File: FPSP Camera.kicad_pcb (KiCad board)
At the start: 4 copper layers, 85.7 x 31.1 mm, 72 parts, among them J1 Conn_01x24_Socket, J2 Conn_02x04_Counter_Clockwise, J3 Conn_02x07_Counter_Clockwise, J7 Conn_01x02, U1 ICM-45686, U3 RP2350_60QFN, U4 TLV75533PDRV, U5 TLV73328PDRV, U6 TLV73315PDRV, Y1 SiT8008xx-1x-xxE

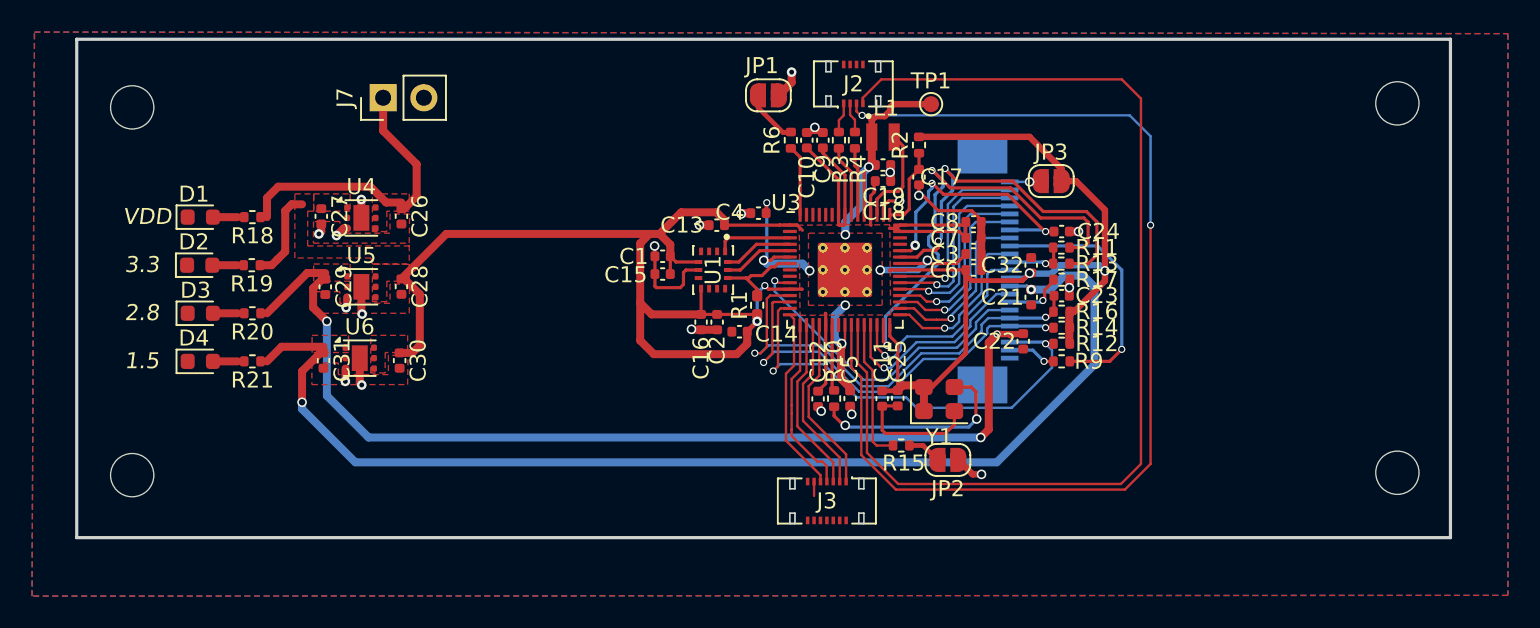
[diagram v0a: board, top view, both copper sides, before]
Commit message: FPC socket foorprint replaced
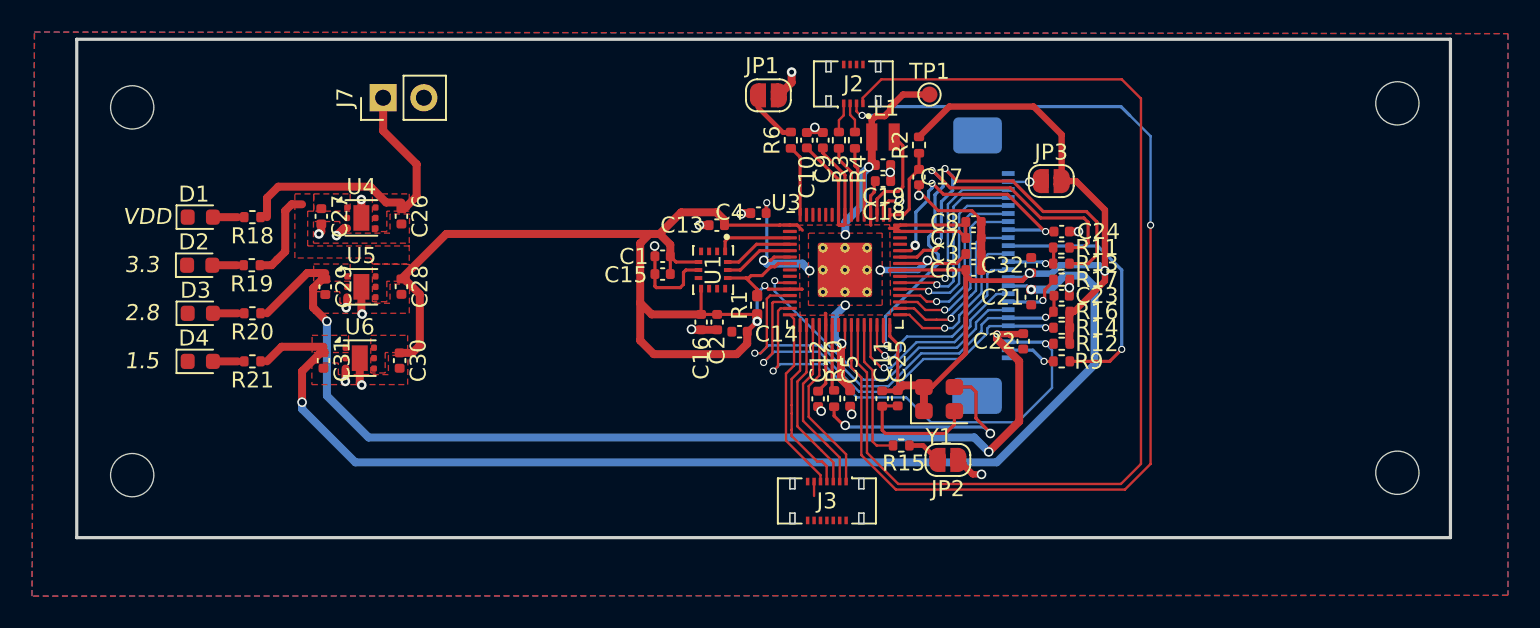
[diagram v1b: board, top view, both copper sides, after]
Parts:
- J1: footprint Connector_FFC-FPC:TE_2-1734839-3_1x23-1MP_P0.5mm_Horizontal -> 52435-2471:MOLEX_52435-2471
- moved J1 1.29 mm to (77.1, 30.0)
- moved TP1 0.61 mm to (72.2, 19.4)
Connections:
- J1 pad MP: (no net) -> AGND
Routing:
- net +3.3V: track 161.3 -> 164.1 mm
- net +2V8: track 64.1 -> 66.8 mm
- net /XIN_mem1: track 13.2 -> 15.2 mm
- net SDA_cam_1: track 29.0 -> 30.5 mm
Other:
- board text added: "Stiffener 1: Polyamide Stiffener 1 Thickness: 0.2mm Stiffener 1 Location: see User.1 layer (for PCB please disregard)"
- board text added: "Stiffener 2: FR4 Stiffener 2 Thickness: 0.2mm Stiffener 2 Location: see User.2 layer (for PCB please disregard)"
- board text removed: "Stiffener 1: Polyamide Stiffener 1 Thickness: 0.2mm Stiffener 1 Location: see User.1 layer"
- board text removed: "Stiffener 2: FR4 Stiffener 2 Thickness: 0.2mm Stiffener 2 Location: see User.2 layer"

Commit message: test PCB version 2 completed
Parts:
- removed the J2 at (67.4, 18.7)
- added J3: Conn_02x07_Counter_Clockwise, Connector_Molex:Molex_SlimStack_502426-1410_2x07_P0.40mm_Vertical, F.Cu at (68.0, 18.4)
- added TP2: TestPoint, TestPoint:TestPoint_Pad_D1.0mm, F.Cu at (88.8, 28.2)
- moved J4 2.85 mm to (63.1, 43.9)
- moved C11 2.09 mm to (70.2, 40.2)
- moved TP1 1.41 mm to (73.6, 19.1)
- moved R15 1.13 mm to (70.7, 42.4)
- renumbered C3 to C1, C4 to C2, C32 to C23, C23 to C24, C24 to C25, C25 to C26, C26 to C27, C27 to C28, C28 to C29, C5 to C3, C29 to C30, C30 to C31, C31 to C32, C1 to C4, C2 to C5, J7 to J2, J3 to J4
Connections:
- J4 pad 1: IMAGE_OUT_1_1+ -> HREF_OUT
- J4 pad 11: AGND -> IMAGE_OUT_1
- J4 pad 13: unconnected-(J3-Pin_13-Pad13) -> FPGA_EN
- J4 pad 14: unconnected-(J3-Pin_14-Pad14) -> AGND
- J4 pad 3: IMAGE_OUT_2_1+ -> POSITION_OUT_1
- J4 pad 4: unconnected-(J3-Pin_4-Pad4) -> IMAGE_CLK
- J4 pad 5: IMAGE_OUT_2_1- -> IMAGE_OUT_4
- J4 pad 6: unconnected-(J3-Pin_6-Pad6) -> VSYNC_OUT
- J4 pad 7: IMAGE_OUT_1_1- -> IMAGE_OUT_3
- J4 pad 8: unconnected-(J3-Pin_8-Pad8) -> POSITION_OUT_CLK
- J4 pad 9: POSITION_OUT_1 -> IMAGE_OUT_2
- U3 pad 15: POSITION_OUT_1 -> FPGA_EN
- U3 pad 16: IMAGE_OUT_1_1- -> IMAGE_OUT_1
- U3 pad 17: IMAGE_OUT_2_1- -> IMAGE_OUT_2
- U3 pad 18: IMAGE_OUT_2_1+ -> IMAGE_OUT_3
- U3 pad 19: IMAGE_OUT_1_1+ -> IMAGE_OUT_4
- U3 pad 27: HSYNC_1 -> IMAGE_CLK
- U3 pad 28: DATA9_1 -> VSYNC_OUT
- U3 pad 29: EXT_XCLK_1 -> POSITION_OUT_CLK
- U3 pad 31: DATA8_1 -> POSITION_OUT_1
- U3 pad 32: DATA7_1 -> HREF_OUT
- U3 pad 33: DATA6_1 -> INT_XCLK
- U3 pad 35: DATA5_1 -> DATA3_1
- U3 pad 36: DATA3_1 -> DATA4_1
- U3 pad 37: DATA4_1 -> DATA5_1
- U3 pad 40: INT_XCLK -> DATA6_1
- U3 pad 41: PCLK_1 -> DATA7_1
- U3 pad 42: unconnected-(U3-GPIO28_ADC2-Pad42) -> DATA8_1
- U3 pad 43: unconnected-(U3-GPIO29_ADC3-Pad43) -> DATA9_1
- U3 pad 8: unconnected-(U3-GPIO5-Pad8) -> PCLK_1
- U3 pad 9: unconnected-(U3-GPIO6-Pad9) -> HSYNC_1
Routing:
- net +5V: track 18.6 -> 48.6 mm
- net POSITION_OUT_CLK: track 0.00 -> 19.8 mm
- net EXT_XCLK_1: track 28.3 -> 8.53 mm
- net VSYNC_OUT: track 0.00 -> 18.6 mm
- net IMAGE_CLK: track 0.00 -> 17.4 mm
- net HREF_OUT: track 0.00 -> 16.7 mm, vias 0 -> 2
- net PCLK_1: track 16.7 -> 31.3 mm
- net IMAGE_OUT_1_1+: track 11.0 -> 0.00 mm
- net IMAGE_OUT_2_1+: track 11.0 -> 0.00 mm
- net IMAGE_OUT_1_1-: track 11.0 -> 0.00 mm
- net IMAGE_OUT_2_1-: track 10.9 -> 0.00 mm
- net HSYNC_1: track 13.1 -> 23.7 mm, vias 1 -> 3
- net FPGA_EN: track 0.00 -> 10.2 mm
- net IMAGE_OUT_3: track 0.00 -> 9.67 mm
- net IMAGE_OUT_4: track 0.00 -> 9.67 mm
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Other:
- board text added: "5V"
- board text added: "FPGA_EN"
- board text added: "GND"

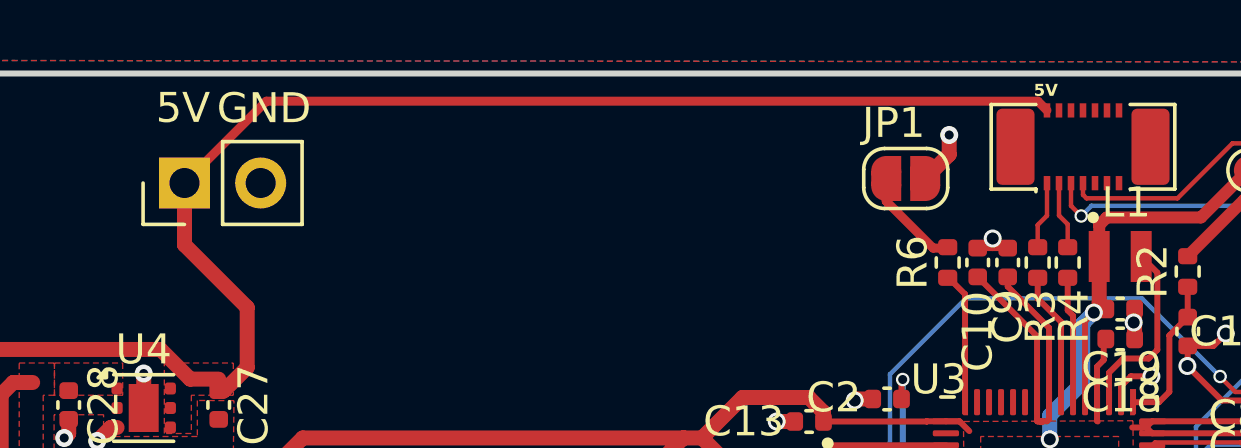
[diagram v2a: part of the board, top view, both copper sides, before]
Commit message: refined 5V net isolation
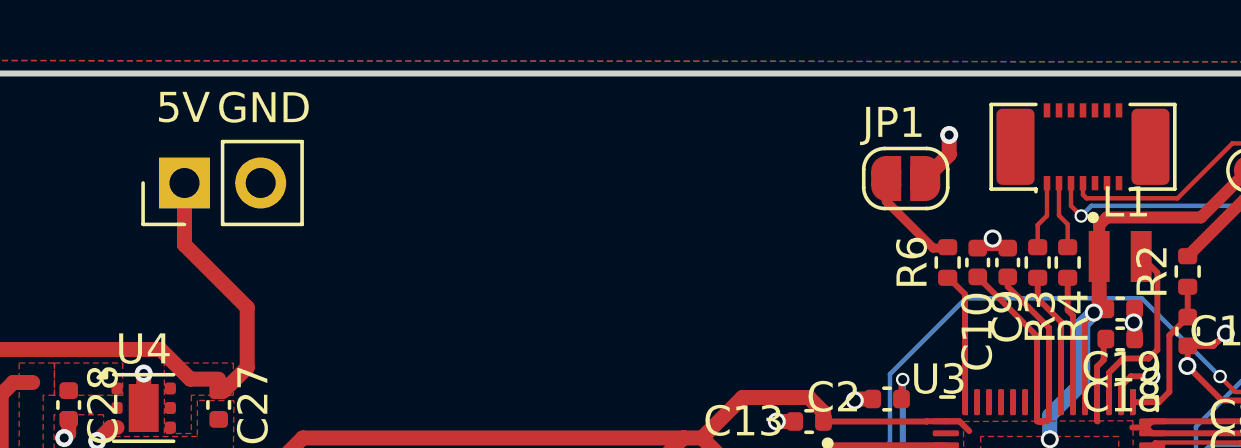
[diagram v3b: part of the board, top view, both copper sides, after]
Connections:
- J3 pad 2: +5V -> unconnected-(J3-Pin_2-Pad2)
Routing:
- net +5V: track 48.6 -> 18.6 mm
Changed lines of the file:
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@@
 			(size 0.22 0.475)
 			(layers "F.Cu" "F.Mask" "F.Paste")
-			(net "+5V")
+			(net "unconnected-(J3-Pin_2-Pad2)")
 			(pinfunction "Pin_2_2")
-			(pintype "passive")
+			(pintype "passive+no_connect")
 		)
 		(pad "3" smd rect
@@
 		)
 	)
-	(gr_text "5V"
-		(at 66.792265 16.479144 0)
-		(layer "F.SilkS")
-		(effects
-			(font
-				(size 0.4 0.4)
-				(thickness 0.1)
-				(bold yes)
-			)
-		)
-	)
 	(gr_text "VDD"
 		(at 21.834765 27.569144 0)
@@
 	)
 	(segment
-		(start 66.524765 16.841644)
-		(end 40.809765 16.841644)
-		(width 0.3)
-		(layer "F.Cu")
-		(net "+5V")
-	)
-	(segment
 		(start 40.172265 25.719144)
 		(end 40.172265 23.719144)
@@
 	)
 	(segment
-		(start 66.832265 17.149144)
-		(end 66.524765 16.841644)
-		(width 0.3)
-		(layer "F.Cu")
-		(net "+5V")
-	)
-	(segment
 		(start 30.834765 27.019144)
 		(end 30.834765 25.819144)
@@
 		(layer "F.Cu")
 		(net "+5V")
-	)
-	(segment
-		(start 40.809765 16.841644)
-		(end 38.082265 19.569144)
-		(width 0.3)
-		(layer "F.Cu")
-		(net "+5V")
